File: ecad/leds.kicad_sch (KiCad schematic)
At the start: 23 parts, among them U4 SN74LV1T34DBV

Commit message: feat(ecad): general routing
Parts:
- added D41, D42, D43, D44, D45, D46, D47, D48: WS2812B-2020, LED_SMD:LED_WS2812B-2020_PLCC4_2.0x2.0mm, symbol LED:WS2812B-2020
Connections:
- net +5V: now also D41.4 (VDD), D42.4 (VDD), D43.4 (VDD), D44.4 (VDD), D45.4 (VDD), D46.4 (VDD), D47.4 (VDD), D48.4 (VDD)
- net GND: now also D41.2 (VSS), D43.2 (VSS), D44.2 (VSS), D45.2 (VSS), D47.2 (VSS), D48.2 (VSS)
- net at D13.3 (DIN): now also D42.1 (DOUT); no longer D17.1 (DOUT)
- net at D15.3 (DIN): now also D44.1 (DOUT); no longer D19.1 (DOUT)
- new net: D44.3 (DIN), D48.1 (DOUT)
- new net: D42.3 (DIN), D46.1 (DOUT)
- new net: D17.1 (DOUT), D41.3 (DIN)
- new net: D19.1 (DOUT), D43.3 (DIN)
- new net: D45.1 (DOUT), D46.3 (DIN)
- new net: D47.1 (DOUT), D48.3 (DIN)
- new net: D41.1 (DOUT), D45.3 (DIN)
- new net: D43.1 (DOUT), D47.3 (DIN)
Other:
- moved on the sheet: C18, D13, D14, D15, D16, D17, D18, D19, D20, D21, D22, D23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

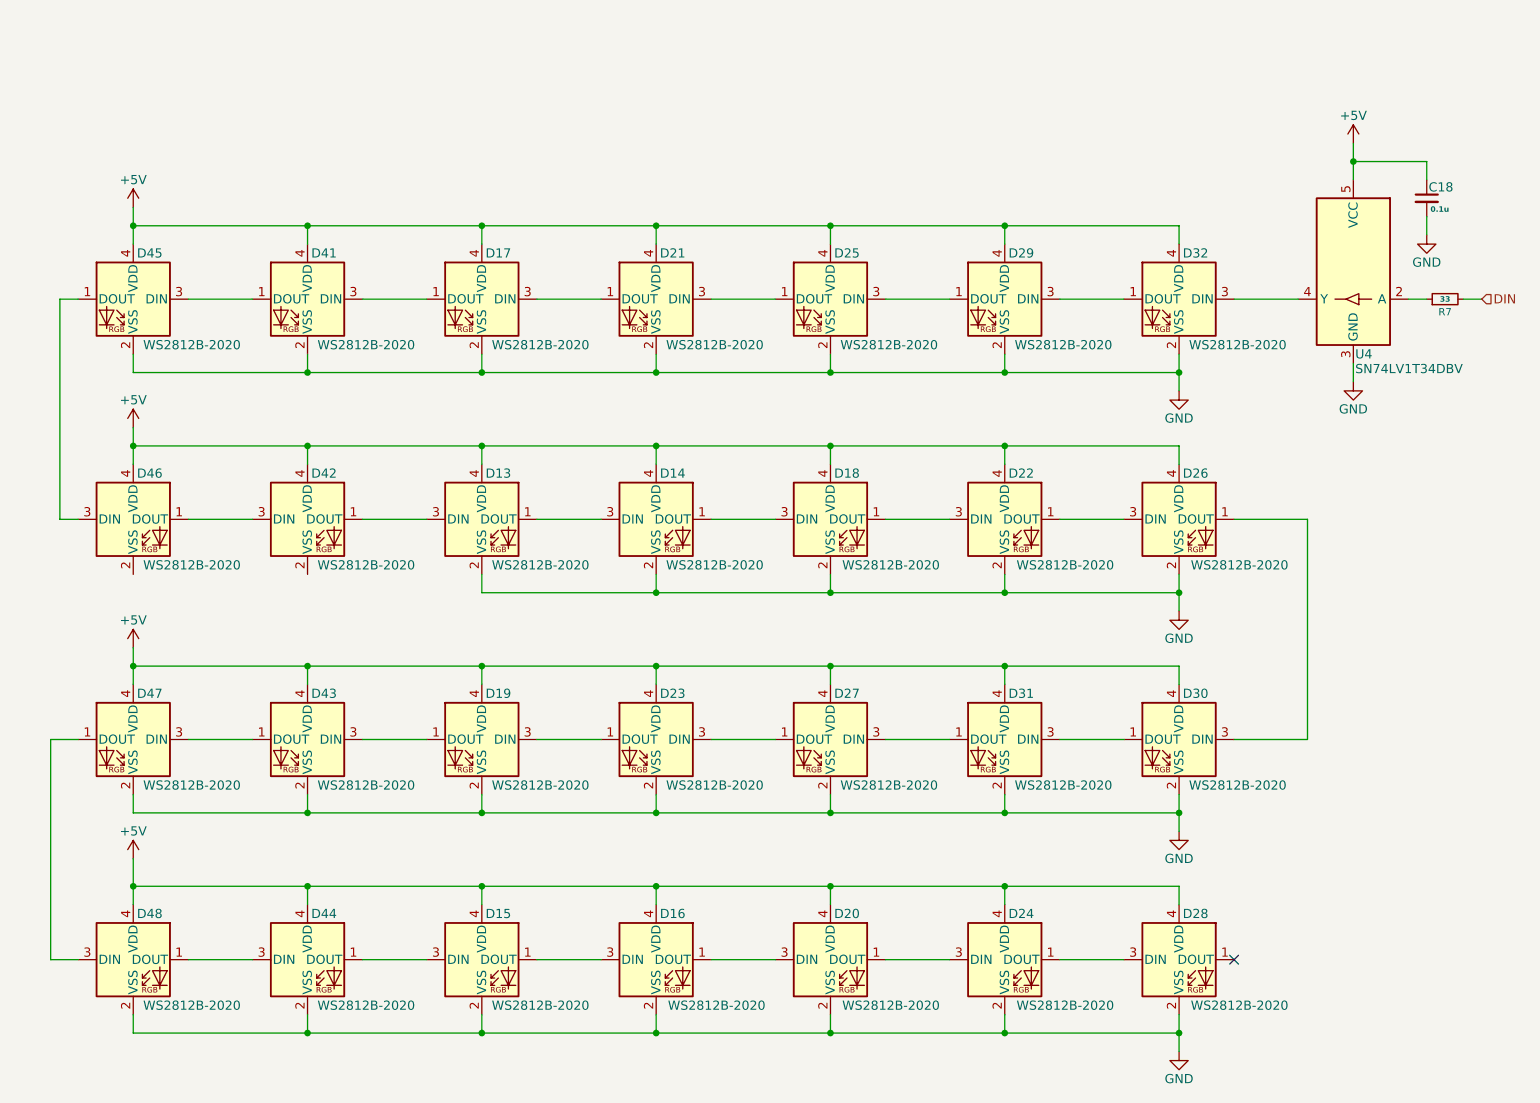
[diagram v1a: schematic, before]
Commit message: feat(ecad): ws2812b placement and routing
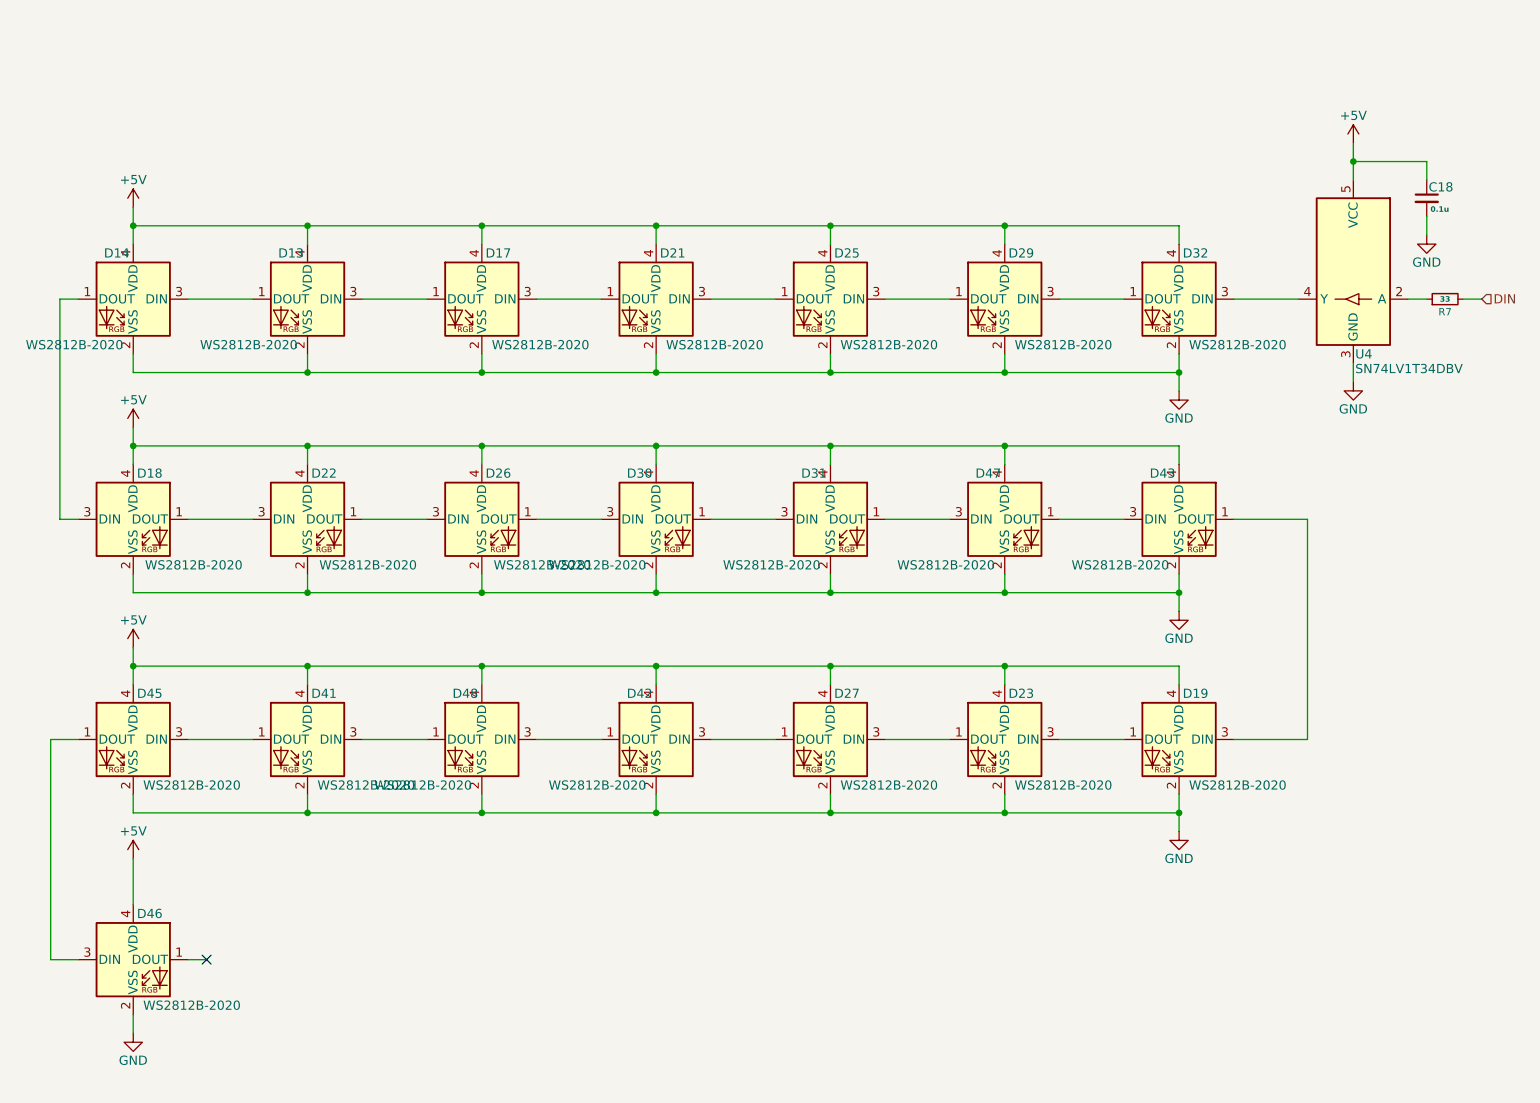
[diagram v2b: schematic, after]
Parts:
- removed D15, D16, D20, D24, D28, D44: WS2812B-2020, LED_SMD:LED_WS2812B-2020_PLCC4_2.0x2.0mm, symbol LED:WS2812B-2020
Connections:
- net GND: now also D42.2 (VSS), D46.2 (VSS)
- net at D48.1 (DOUT): now also D41.3 (DIN)
- net at D42.1 (DOUT): now also D48.3 (DIN); no longer D13.3 (DIN)
- net at D42.3 (DIN): now also D27.1 (DOUT); no longer D46.1 (DOUT)
- net at D17.1 (DOUT): now also D13.3 (DIN); no longer D41.3 (DIN)
- net at D19.1 (DOUT): now also D23.3 (DIN); no longer D43.3 (DIN)
- net at D19.3 (DIN): now also D43.1 (DOUT); no longer D23.1 (DOUT)
- net at D47.1 (DOUT): now also D43.3 (DIN); no longer D48.3 (DIN)
- net at D27.3 (DIN): now also D23.1 (DOUT); no longer D31.1 (DOUT)
- net at D47.3 (DIN): now also D31.1 (DOUT); no longer D43.1 (DOUT)
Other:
- moved on the sheet: D13, D14, D18, D19, D22, D23, D26, D30, D31, D41, D42, D43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
